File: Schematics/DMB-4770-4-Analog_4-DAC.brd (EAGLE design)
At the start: 32.8 x 86.9 mm, 70 parts

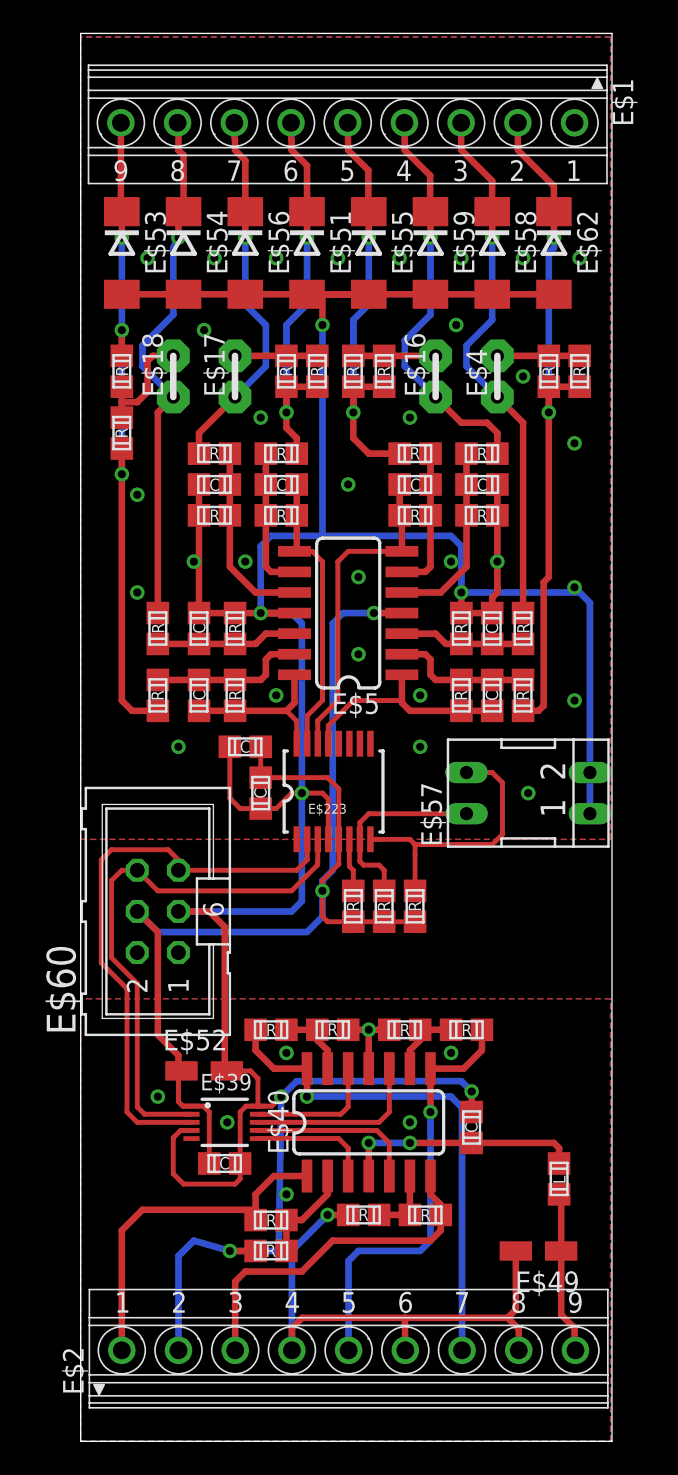
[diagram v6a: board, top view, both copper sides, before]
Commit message: Modification empreintes resistances
Au lieu de 2 resistances 500, une seule 250 en 1206
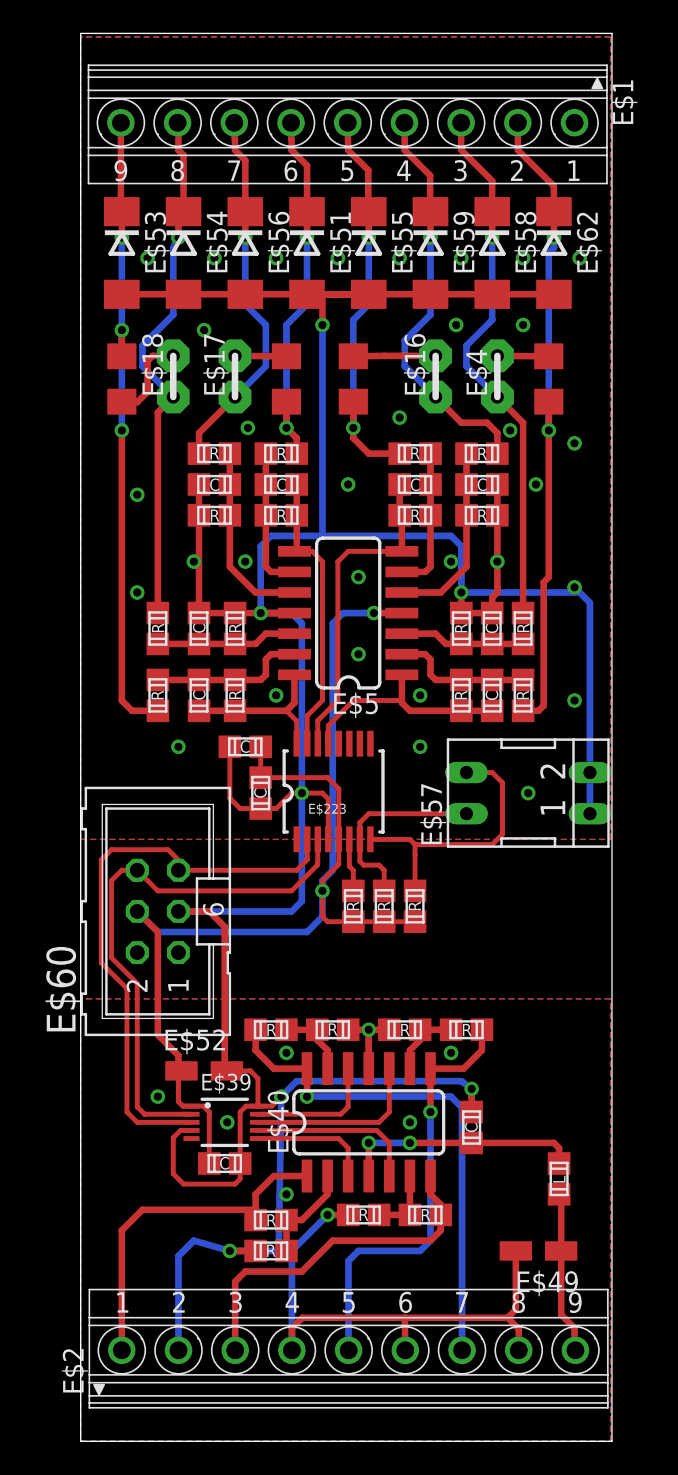
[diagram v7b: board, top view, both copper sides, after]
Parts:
- removed E$20, E$63, E$64, E$65: 500, divers:R0805
- E$19, E$66, E$7, E$8: device divers:R0805 -> SparkFun-Resistors:1206
- moved E$19 0.48 mm to (12.7, 65.6)
- moved E$66 0.48 mm to (2.54, 65.6)
- moved E$7 0.48 mm to (28.9, 65.6)
- moved E$8 0.48 mm to (16.8, 65.6)
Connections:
- net IN1-: no longer E$20.2
- net IN2-: no longer E$65.2
- net IN3-: no longer E$64.2
- net IN4-: no longer E$63.2
- net S$10: no longer E$63.1
- net S$15: no longer E$20.1
- net S$20: no longer E$65.1
- net S$21: no longer E$64.1
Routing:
- net S$20: track 5.08 -> 3.18 mm
- net S$10: track 5.08 -> 3.18 mm
- net S$15: track 7.38 -> 5.50 mm
- net IN3-: track 27.1 -> 25.2 mm
- net IN2-: track 25.1 -> 23.2 mm
- net IN4-: track 42.1 -> 40.3 mm
- net IN1-: track 41.3 -> 39.8 mm
- net GND: vias 45 -> 47
